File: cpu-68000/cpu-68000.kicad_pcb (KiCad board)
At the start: 4 copper layers, 160 x 100 mm, 129 parts, among them J101 Conn_02x04_Odd_Even, J201 Conn_03x32_Row_Letter_First, J502 DB9_Male_MountingHoles, J503 Conn_02x03_Odd_Even, SW501 SW_DIP_x05, SW502 Blue, SW503 Black, U101 ATF22V10C, U102 ATF22V10C, U103 74HC175, U104 74HC05, U201 SN74LVCH16T245, U202 SN74LVCH16T245, U203 SN74LXC8T245, U204 SN74LVC2T45, U205 SN74LVC2T45, U301 MC68000FN, U302 74HC2G08DC, U303 TL7733B, U304 74HC175, U305 ATF22V10C, U306 74HC148, U401 IS61C5128AL-10TLI, U402 IS61C5128AL-10TLI, U403 IS61C5128AL-10TLI, U404 IS61C5128AL-10TLI, U501 74HC2G14, U502 74HCT2G04, U503 XR68C681, U504 PCF8584, U505 DS1744, U506 MAX202, U507 SAA1099, U508 SAA1099, X101 10MHz, Y501 3.6864MHz, Y502 7.15909MHz

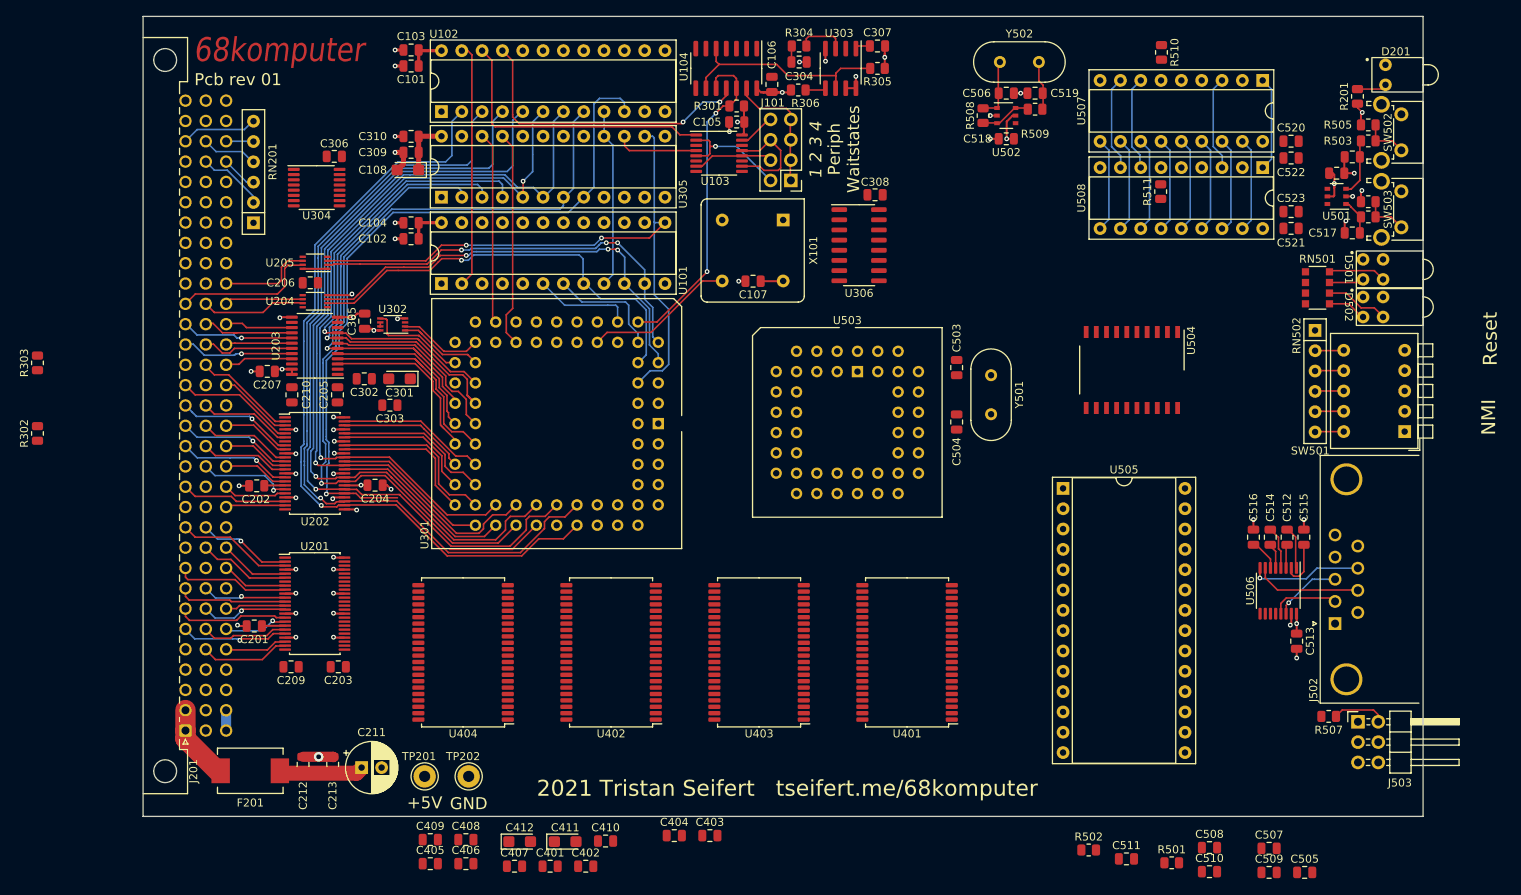
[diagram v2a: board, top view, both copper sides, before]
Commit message: More control signals; start RAM routing
- Started routing the address/data bus for the RAM, including some
  rejigging of the data bus layout

- Added a fuse and power conditioning for 12V, to be used for the analog
  section on the sound side
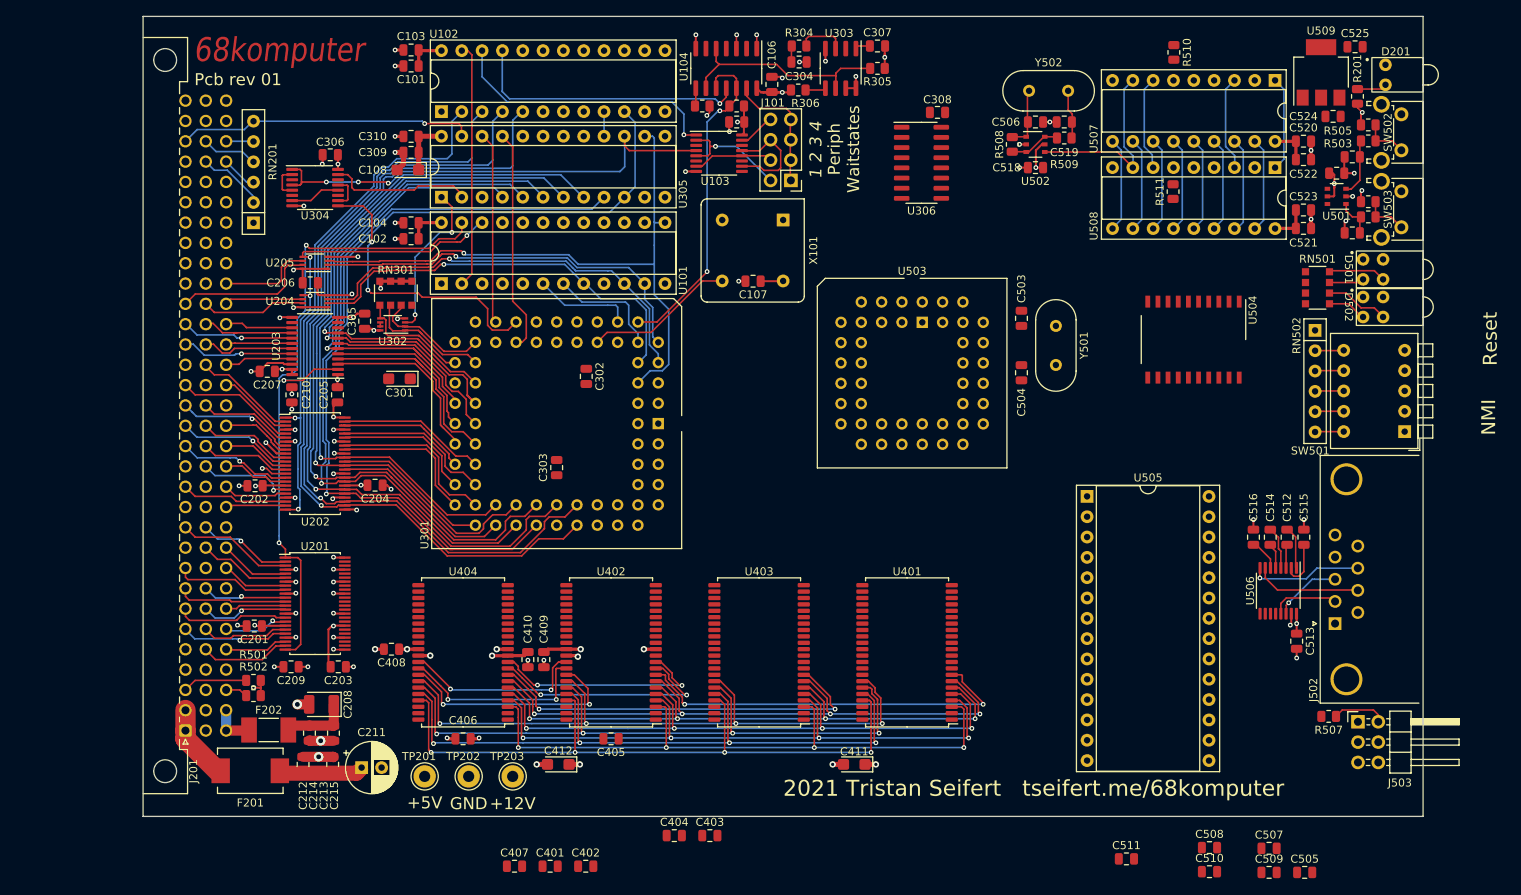
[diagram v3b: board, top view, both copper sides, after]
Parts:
- removed R303: 10k, Resistor_SMD:R_0805_2012Metric
- added C208: 10µF, Capacitor_Tantalum_SMD:CP_EIA-3528-21_Kemet-B, F.Cu at (42.3, 106.0)
- added C214: 1µF, Capacitor_SMD:C_0805_2012Metric, F.Cu at (40.8, 109.6)
- added C215: 100nF, Capacitor_SMD:C_0805_2012Metric, F.Cu at (43.8, 109.6)
- added C524: 1µF, Capacitor_SMD:C_0805_2012Metric, F.Cu at (168.8, 32.5)
- added C525: 4.7µF, Capacitor_SMD:C_0805_2012Metric, F.Cu at (171.5, 23.8)
- added F202: .1A, Fuse:Fuse_Littelfuse-NANO2-451_453, F.Cu at (35.7, 109.2)
- added RN301: 10k, Resistor_SMD:R_Array_Convex_4x1206, F.Cu at (51.6, 54.6)
- added TP203: TestPoint, TestPoint:TestPoint_Loop_D2.60mm_Drill1.4mm_Beaded, F.Cu at (66.2, 115.0)
- added U509: LDL1117S50R, Package_TO_SOT_SMD:SOT-223-3_TabPin2, F.Cu at (167.2, 27.0)
- moved R501 117.0 mm to (33.8, 103.0)
- moved R502 106.2 mm to (33.8, 104.9)
- moved R302 92.6 mm to (89.9, 31.2), turned to 180 degrees
- moved C411 37.4 mm to (108.9, 113.5), turned to 180 degrees
- moved C302 27.8 mm to (75.4, 65.0), turned to -90 degrees
- moved C405 27.5 mm to (78.5, 110.3), turned to 180 degrees
- moved C409 26.6 mm to (70.1, 100.4), turned to -90 degrees
- moved C408 25.6 mm to (51.0, 99.1), turned to 180 degrees
- moved C410 24.7 mm to (68.1, 100.4), turned to -90 degrees
- moved C303 22.3 mm to (71.7, 76.4), turned to 90 degrees
- moved C406 15.6 mm to (60.0, 110.3), turned to 180 degrees
- moved U306 12.9 mm to (117.3, 38.3)
- moved C308 12.9 mm to (119.3, 32.0)
- moved C412 10.8 mm to (71.9, 113.5), turned to 180 degrees
- moved U503 10.2 mm to (117.4, 58.2)
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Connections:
- net +12V renamed Net-(J201-Padc1)
- J201 pad a11: /Backplane Connection/BD14 -> /Backplane Connection/BD6
- J201 pad a6: /Backplane Connection/BD2 -> /Backplane Connection/BD10
- J201 pad a7: /Backplane Connection/BD5 -> /Backplane Connection/BD13
- J201 pad a8: /Backplane Connection/BD8 -> /Backplane Connection/BD0
- J201 pad a9: /Backplane Connection/BD10 -> /Backplane Connection/BD2
- J201 pad b10: /Backplane Connection/BD12 -> /Backplane Connection/BD4
- J201 pad b11: /Backplane Connection/BD15 -> /Backplane Connection/BD7
- J201 pad b5: /Backplane Connection/BD0 -> /Backplane Connection/BD8
- J201 pad b6: /Backplane Connection/BD3 -> /Backplane Connection/BD11
- J201 pad b7: /Backplane Connection/BD6 -> /Backplane Connection/BD14
- J201 pad b8: /Backplane Connection/BD9 -> /Backplane Connection/BD1
- J201 pad c10: /Backplane Connection/BD13 -> /Backplane Connection/BD5
- J201 pad c5: /Backplane Connection/BD1 -> /Backplane Connection/BD9
- J201 pad c6: /Backplane Connection/BD4 -> /Backplane Connection/BD12
- J201 pad c7: /Backplane Connection/BD7 -> /Backplane Connection/BD15
- J201 pad c9: /Backplane Connection/BD11 -> /Backplane Connection/BD3
- R302 pad 2: /~{BR} -> /Main CPU/~{HALT}
- U201 pad 11: /Backplane Connection/BD9 -> /Backplane Connection/BD1
- U201 pad 12: /Backplane Connection/BD8 -> /Backplane Connection/BD0
- U201 pad 13: /Backplane Connection/BD7 -> /Backplane Connection/BD15
- U201 pad 14: /Backplane Connection/BD6 -> /Backplane Connection/BD14
- U201 pad 16: /Backplane Connection/BD5 -> /Backplane Connection/BD13
- U201 pad 17: /Backplane Connection/BD4 -> /Backplane Connection/BD12
- U201 pad 19: /Backplane Connection/BD3 -> /Backplane Connection/BD11
- U201 pad 2: /Backplane Connection/BD15 -> /Backplane Connection/BD7
- U201 pad 20: /Backplane Connection/BD2 -> /Backplane Connection/BD10
- U201 pad 22: /Backplane Connection/BD1 -> /Backplane Connection/BD9
- U201 pad 23: /Backplane Connection/BD0 -> /Backplane Connection/BD8
- U201 pad 26: /D0 -> /D15
- U201 pad 27: /D1 -> /D8
- U201 pad 29: /D2 -> /D14
- U201 pad 3: /Backplane Connection/BD14 -> /Backplane Connection/BD6
- U201 pad 30: /D3 -> /D9
- U201 pad 32: /D4 -> /D13
- U201 pad 33: /D5 -> /D10
- U201 pad 35: /D6 -> /D12
- U201 pad 36: /D7 -> /D11
- U201 pad 37: /D8 -> /D0
- U201 pad 38: /D9 -> /D1
- U201 pad 40: /D10 -> /D2
- U201 pad 41: /D11 -> /D3
- U201 pad 43: /D12 -> /D4
- U201 pad 44: /D13 -> /D5
- U201 pad 46: /D14 -> /D6
- U201 pad 47: /D15 -> /D7
- U201 pad 5: /Backplane Connection/BD13 -> /Backplane Connection/BD5
- U201 pad 6: /Backplane Connection/BD12 -> /Backplane Connection/BD4
- U201 pad 8: /Backplane Connection/BD11 -> /Backplane Connection/BD3
- U201 pad 9: /Backplane Connection/BD10 -> /Backplane Connection/BD2
- U305 pad 1: /~{EXT_BERR} -> /Main CPU/CPUSPACE
- U305 pad 10: unconnected-(U305-Pad10) -> /A19
- U305 pad 11: /Main CPU/BUS_TIMEOUT -> unconnected-(U305-Pad11)
- U305 pad 2: /A2 -> /Main CPU/BUS_TIMEOUT
- U305 pad 3: /A3 -> /~{EXT_BERR}
- U305 pad 4: /A1 -> /A2
- U305 pad 5: /A16 -> /A3
- U305 pad 6: /A18 -> /A1
- U305 pad 7: /A17 -> /A16
- U305 pad 8: /A19 -> /A18
- U305 pad 9: /Main CPU/CPUSPACE -> /A17
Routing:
- net /A19: track 102.4 -> 196.4 mm, vias 1 -> 5
- net /A18: track 101.7 -> 191.2 mm, vias 1 -> 5
- net /A17: track 102.0 -> 190.3 mm, vias 1 -> 5
- net /A16: track 92.6 -> 180.5 mm, vias 2 -> 5
- net /A1: track 70.2 -> 155.4 mm, vias 1 -> 5
- net /A2: track 54.0 -> 138.7 mm, vias 1 -> 5
- net /A3: track 58.7 -> 142.1 mm, vias 1 -> 5
- net /A5: track 23.2 -> 102.8 mm, vias 0 -> 4
- net /DBUF_DIR: track 0.00 -> 77.9 mm, vias 0 -> 2
- net /A4: track 21.2 -> 98.9 mm, vias 0 -> 4
- net /ABUF_DIR: track 0.00 -> 71.9 mm, vias 0 -> 6
- net GND: track 76.2 -> 135.9 mm, vias 49 -> 76
- net +5V: track 79.3 -> 134.2 mm, vias 12 -> 32
- net /~{RAM2_CS}: track 0.00 -> 49.8 mm, vias 0 -> 2
- net /~{RAM1_CS}: track 0.00 -> 49.5 mm, vias 0 -> 2
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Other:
- board text added: "+12V"
